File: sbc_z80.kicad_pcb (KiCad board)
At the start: 2 copper layers, 101.6 x 50.8 mm, 19 parts, among them J1 Conn_02x40_Top_Bottom, J2 UPDI TTL, U1 Z84C4310AEG, U10 74HC3G34DP,125, U2 Si5351A-B-GT, U3 IS62C5128BL-45TLI, U4 27C512PLCC, U5 ATtiny1614-SS, U6 Z84C0010AEG, U7 EPM7032STC44, U8 Z84C3010AEG, U9 Z84C2010AEG, Y1 25MHZ 8PF

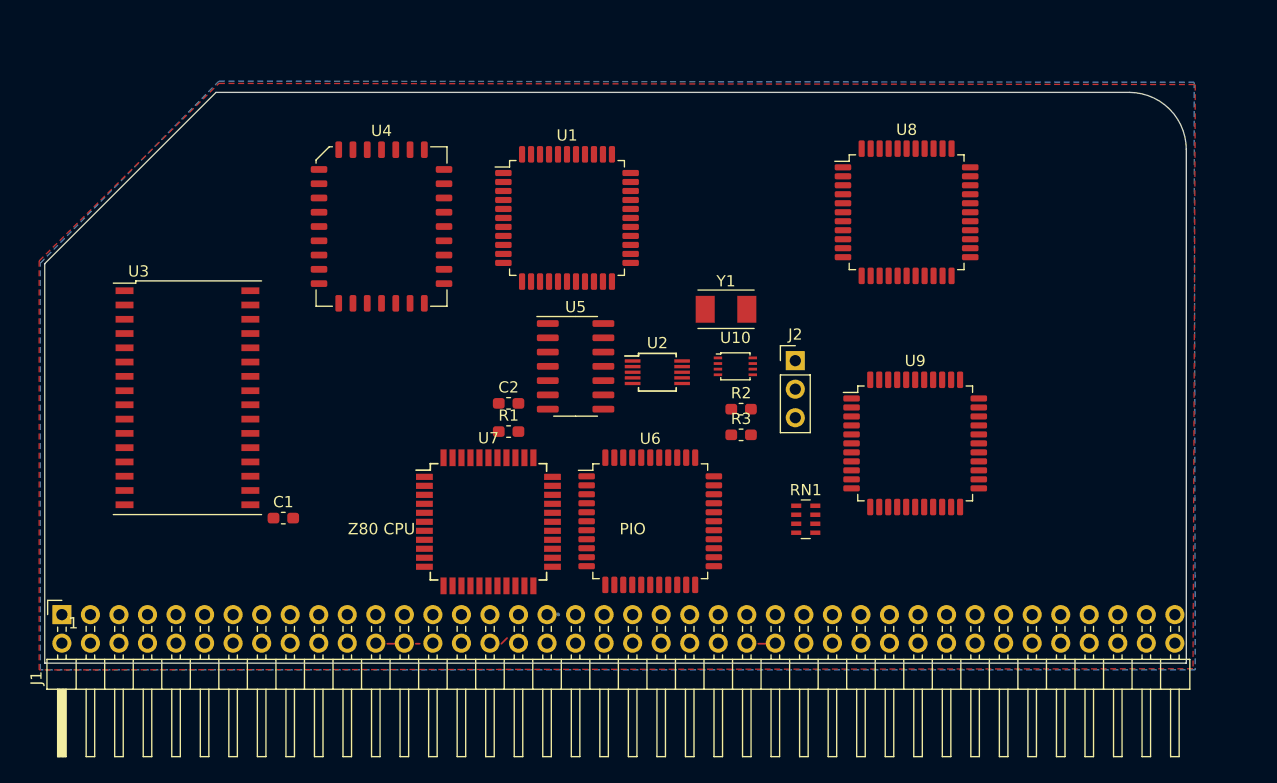
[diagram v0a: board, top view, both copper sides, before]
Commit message: added 3V3 section for clock generator
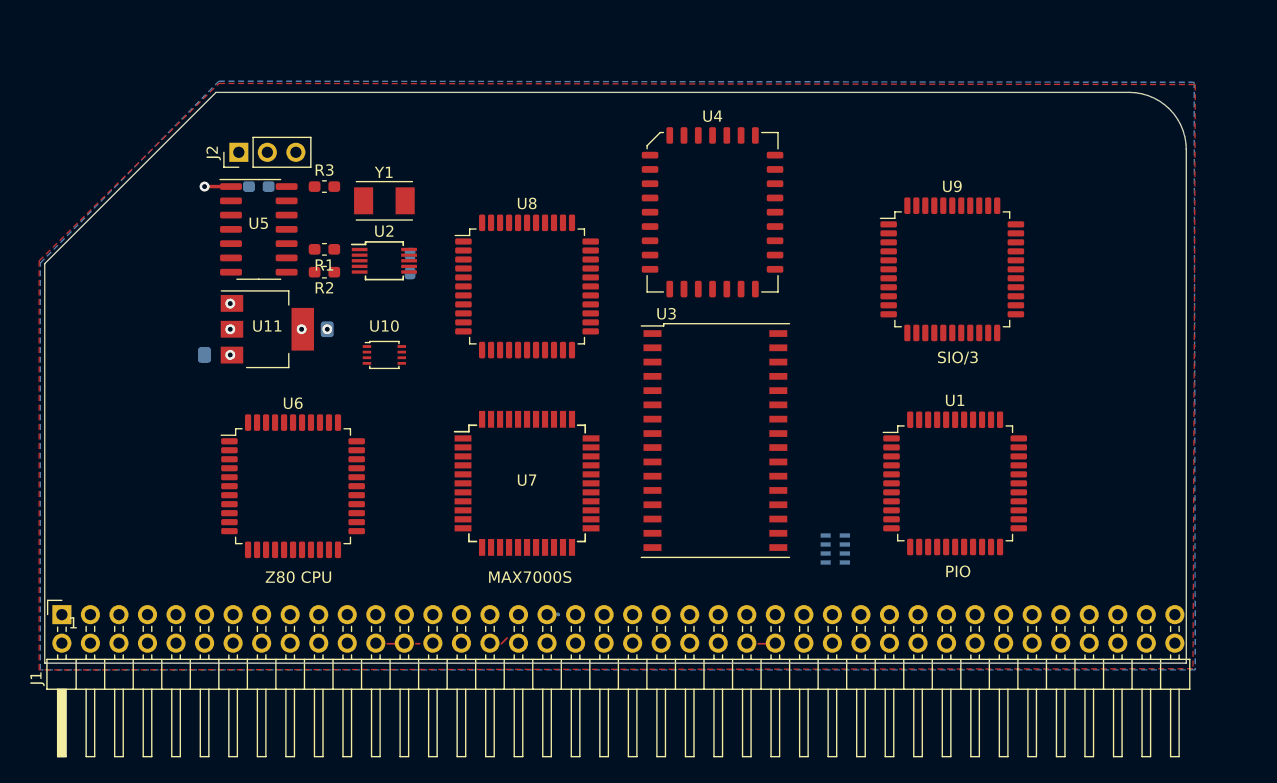
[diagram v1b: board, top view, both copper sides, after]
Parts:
- added C3: 10uF, Capacitor_SMD:C_0805_2012Metric_Pad1.15x1.40mm_HandSolder, B.Cu at (90.7, 100.1)
- added C4: 22uF, Capacitor_SMD:C_0805_2012Metric_Pad1.15x1.40mm_HandSolder, B.Cu at (99.6, 97.8)
- added U11: AZ1117CH-3.3TRG1, Package_TO_SOT_SMD:SOT-223-3_TabPin2, F.Cu at (95.2, 97.8)
- C1, C2, RN1: moved to B.Cu
- moved J2 52.9 mm to (92.7, 82.0), turned to 90 degrees
- moved U3 47.1 mm to (135.1, 107.7)
- moved R3 43.2 mm to (100.3, 85.1)
- moved U1 41.8 mm to (156.5, 111.5)
- moved R2 39.0 mm to (100.3, 92.7), turned to 180 degrees
- moved U8 34.4 mm to (118.4, 94.0)
- moved U6 31.9 mm to (97.5, 111.8)
- moved Y1 31.9 mm to (105.7, 86.4)
- moved U10 31.3 mm to (105.7, 100.1)
- moved U5 30.7 mm to (94.5, 88.9)
- moved U4 29.5 mm to (134.9, 87.4)
- moved C2 29.4 mm to (94.5, 85.1)
- moved U2 26.2 mm to (105.7, 91.7)
- moved C1 25.3 mm to (108.0, 91.9), turned to 90 degrees
- moved R1 23.1 mm to (100.3, 90.7), turned to 180 degrees
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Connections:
- J1 pad 23: (no net) -> /~MREQ
- J1 pad 24: (no net) -> /~WR
- J1 pad 25: (no net) -> /~RD
- J1 pad 26: (no net) -> /~IORQ
- J1 pad 54: (no net) -> /A18
- J1 pad 55: (no net) -> /A17
- J1 pad 56: (no net) -> /A16
- U1 pad 20: (no net) -> /A0
- U1 pad 21: (no net) -> /A1
- U1 pad 5: (no net) -> /CLK
- U3 pad 1: (no net) -> /A17
- U3 pad 2: (no net) -> /A16
- U3 pad 30: (no net) -> /A18
- U7 pad 1: /A3 -> (no net)
- U7 pad 10: (no net) -> /~RD
- U7 pad 11: (no net) -> /~WR
- U7 pad 12: (no net) -> /~MREQ
- U7 pad 13: (no net) -> /A7
- U7 pad 14: (no net) -> /A7
- U7 pad 15: (no net) -> /A7
- U7 pad 2: /A4 -> /A3
- U7 pad 3: /A5 -> /A4
- U7 pad 5: /A6 -> /A5
- U7 pad 6: /A7 -> /A6
- U7 pad 8: (no net) -> /~IORQ
- U9 pad 11: (no net) -> /A1
- U9 pad 12: (no net) -> /A0
- U9 pad 33: (no net) -> /CLK
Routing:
- net 3V3: track 0.00 -> 2.35 mm, vias 0 -> 3
- net GND: vias 0 -> 2
- net 5V: vias 0 -> 1
- added copper zone on In2.Cu, net 3V3
- added copper zone on In2.Cu, net 5V
- added copper zone on In1.Cu, net GND
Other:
- copper layers 2 -> 4
- board text added: "MAX7000S"
- board text added: "SIO/3"

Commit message: larger sheet, connected more pins
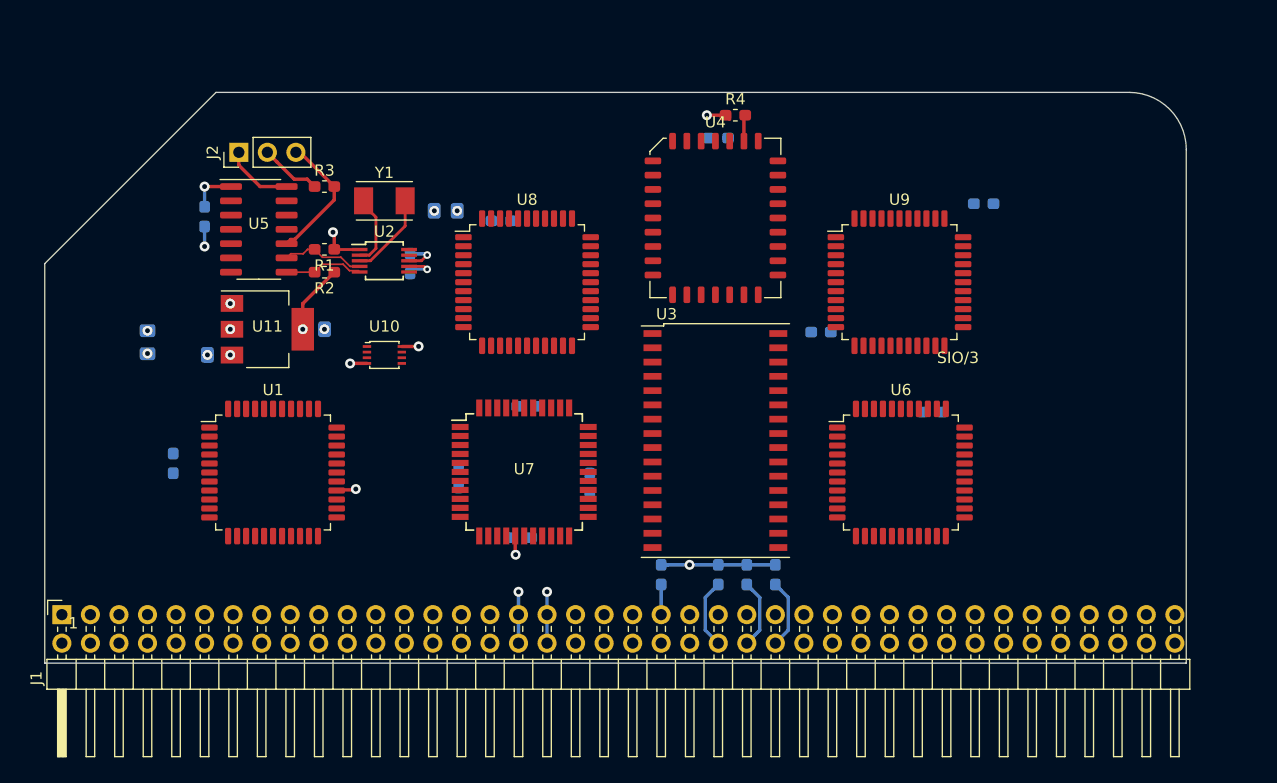
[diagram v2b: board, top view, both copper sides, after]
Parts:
- removed RN1: 10K, Resistor_SMD:R_Array_Concave_4x0603
- added C10: 100nF, Capacitor_SMD:C_0603_1608Metric_Pad1.05x0.95mm_HandSolder, B.Cu at (144.5, 98.0)
- added C11: 100nF, Capacitor_SMD:C_0603_1608Metric_Pad1.05x0.95mm_HandSolder, B.Cu at (154.4, 105.2)
- added C12: 100nF, Capacitor_SMD:C_0603_1608Metric_Pad1.05x0.95mm_HandSolder, B.Cu at (159.0, 86.6)
- added C13: 100nF, Capacitor_SMD:C_0603_1608Metric_Pad1.05x0.95mm_HandSolder, B.Cu at (135.4, 80.8)
- added C14: 100nF, Capacitor_SMD:C_0603_1608Metric_Pad1.05x0.95mm_HandSolder, B.Cu at (116.1, 88.1)
- added C15: 100nF, Capacitor_SMD:C_0805_2012Metric_Pad1.15x1.40mm_HandSolder, B.Cu at (84.6, 98.9)
- added C16: 100nF, Capacitor_SMD:C_0805_2012Metric_Pad1.15x1.40mm_HandSolder, B.Cu at (111.1, 87.2)
- added C5: 100nF, Capacitor_SMD:C_0603_1608Metric_Pad1.05x0.95mm_HandSolder, B.Cu at (118.4, 104.6)
- added C6: 100nF, Capacitor_SMD:C_0603_1608Metric_Pad1.05x0.95mm_HandSolder, B.Cu at (112.3, 111.0)
- added C7: 100nF, Capacitor_SMD:C_0603_1608Metric_Pad1.05x0.95mm_HandSolder, B.Cu at (124.0, 111.5)
- added C8: 100nF, Capacitor_SMD:C_0603_1608Metric_Pad1.05x0.95mm_HandSolder, B.Cu at (117.9, 116.3)
- added C9: 100nF, Capacitor_SMD:C_0603_1608Metric_Pad1.05x0.95mm_HandSolder, B.Cu at (86.9, 109.7)
- added R4: 10K, Resistor_SMD:R_0603_1608Metric_Pad1.05x0.95mm_HandSolder, F.Cu at (136.9, 78.7)
- added R5: 10K, Resistor_SMD:R_0603_1608Metric_Pad1.05x0.95mm_HandSolder, B.Cu at (130.3, 119.6)
- added R6: 10K, Resistor_SMD:R_0603_1608Metric_Pad1.05x0.95mm_HandSolder, B.Cu at (140.5, 119.6)
- added R7: 10K, Resistor_SMD:R_0603_1608Metric_Pad1.05x0.95mm_HandSolder, B.Cu at (137.9, 119.6)
- added R8: 10K, Resistor_SMD:R_0603_1608Metric_Pad1.05x0.95mm_HandSolder, B.Cu at (135.4, 119.6)
- J1: value Conn_02x40_Top_Bottom -> RC80 Bus
- U1: value Z84C4310AEG -> CPU - Z84C0010AEG
- U3: value IS62C5128BL-45TLI -> SRAM - IS62C5128BL-45TLI
- U4: value 27C512PLCC -> ROM - GLS29EE512
- U6: value Z84C0010AEG -> SIO/3 - Z84C4310AEG
- U7: value EPM7032STC44 -> CPLD - EPM7032STC44
- U8: value Z84C3010AEG -> CTC - Z84C3010AEG
- U9: value Z84C2010AEG -> PIO - Z84C2010AEG
- moved U1 60.7 mm to (95.8, 110.5)
- moved U6 54.1 mm to (151.6, 110.5)
- moved C2 5.52 mm to (89.7, 87.8), turned to 270 degrees
- moved U9 4.84 mm to (151.5, 93.6)
- moved U7 1.05 mm to (118.1, 110.5)
- moved U4 0.57 mm to (135.1, 87.9)
- moved U8 0.38 mm to (118.4, 93.6)
- moved C3 0.26 mm to (90.9, 100.1)
- moved C4 0.25 mm to (99.3, 97.8)
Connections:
- net 3V3 renamed +3V3
- C3 pad 1: 5V -> +5V
- J1 pad 18: 5V -> +5V
- J1 pad 19: (no net) -> /~M1
- J1 pad 20: (no net) -> /~RESET
- J1 pad 40: (no net) -> /IEO
- J1 pad 58: 5V -> +5V
- J1 pad 62: (no net) -> /~BUSACK
- J1 pad 63: (no net) -> /~HALT
- J1 pad 64: /~BUSRQ -> /~BUSREQ
- J1 pad 80: (no net) -> /IEI
- U1 pad 1: (no net) -> /CLK
- U1 pad 10: (no net) -> /D1
- U1 pad 11: (no net) -> Net-(U1-Pad11)
- U1 pad 12: (no net) -> /~INT
- U1 pad 13: (no net) -> /~NMI
- U1 pad 14: (no net) -> /~HALT
- U1 pad 15: (no net) -> /~MREQ
- U1 pad 16: (no net) -> /~IORQ
- U1 pad 17: Net-(U1-Pad17) -> Net-(U1-Pad11)
- U1 pad 18: GND -> /~RD
- U1 pad 19: (no net) -> /~WR
- U1 pad 2: (no net) -> /D4
- U1 pad 20: /A0 -> /~BUSACK
- U1 pad 21: /A1 -> /~WAIT
- U1 pad 22: (no net) -> /~BUSREQ
- U1 pad 23: (no net) -> /~RESET
- U1 pad 24: /D6 -> /~M1
- U1 pad 25: /D4 -> (no net)
- U1 pad 26: /D2 -> GND
- U1 pad 27: /D0 -> /A0
- U1 pad 28: Net-(U1-Pad17) -> /A1
- U1 pad 29: /D1 -> /A2
- U1 pad 3: (no net) -> /D3
- U1 pad 30: /D3 -> /A3
- U1 pad 31: /D5 -> /A4
- U1 pad 32: /D7 -> /A5
- U1 pad 33: (no net) -> Net-(U1-Pad11)
- U1 pad 34: (no net) -> /A6
- U1 pad 35: (no net) -> /A7
- U1 pad 36: (no net) -> /A8
- U1 pad 37: 5V -> /A9
- U1 pad 38: (no net) -> /A10
- U1 pad 39: Net-(U1-Pad17) -> Net-(U1-Pad11)
- U1 pad 4: (no net) -> /D5
- U1 pad 40: (no net) -> /A11
- U1 pad 41: (no net) -> /A12
- U1 pad 42: (no net) -> /A13
- U1 pad 43: (no net) -> /A14
- U1 pad 44: (no net) -> /A15
- U1 pad 5: /CLK -> /D6
- U1 pad 6: (no net) -> +5V
- U1 pad 7: (no net) -> /D2
- U1 pad 8: (no net) -> /D7
- U1 pad 9: (no net) -> /D0
- U10 pad 8: 5V -> +5V
- U11 pad 3: 5V -> +5V
- U3 pad 24: (no net) -> /~RD
- U3 pad 29: (no net) -> /~WR
- U3 pad 32: 5V -> +5V
- U4 pad 1: (no net) -> Net-(U4-Pad1)
- U4 pad 10: /A1 -> /A2
- U4 pad 11: /A0 -> /A1
- U4 pad 12: (no net) -> /A0
- U4 pad 16: (no net) -> GND
- U4 pad 17: (no net) -> /D3
- U4 pad 18: /D3 -> /D4
- U4 pad 19: /D4 -> /D5
- U4 pad 2: /A15 -> Net-(U4-Pad1)
- U4 pad 20: /D5 -> /D6
- U4 pad 21: /D6 -> /D7
- U4 pad 22: /D7 -> (no net)
- U4 pad 23: (no net) -> /A10
- U4 pad 24: /A10 -> /~RD
- U4 pad 25: (no net) -> /A11
- U4 pad 26: (no net) -> /A9
- U4 pad 27: /A11 -> /A8
- U4 pad 28: /A9 -> /A13
- U4 pad 29: /A8 -> /A14
- U4 pad 3: /A12 -> /A15
- U4 pad 30: /A13 -> Net-(U4-Pad1)
- U4 pad 31: /A14 -> Net-(R4-Pad2)
- U4 pad 32: 5V -> +5V
- U4 pad 4: /A7 -> /A12
- U4 pad 5: /A6 -> /A7
- U4 pad 6: /A5 -> /A6
- U4 pad 7: /A4 -> /A5
- U4 pad 8: /A3 -> /A4
- U4 pad 9: /A2 -> /A3
- U6 pad 10: /D1 -> (no net)
- U6 pad 17: (no net) -> Net-(U6-Pad17)
- U6 pad 18: (no net) -> GND
- U6 pad 19: (no net) -> /~RD
- U6 pad 2: /D4 -> (no net)
- U6 pad 20: (no net) -> /A0
- U6 pad 21: (no net) -> /A1
- U6 pad 23: (no net) -> /~IORQ
- U6 pad 24: (no net) -> /D6
- U6 pad 25: (no net) -> /D4
- U6 pad 26: GND -> /D2
- U6 pad 27: /A0 -> /D0
- U6 pad 28: /A1 -> Net-(U6-Pad17)
- U6 pad 29: /A2 -> /D1
- U6 pad 3: /D3 -> (no net)
- U6 pad 30: /A3 -> /D3
- U6 pad 31: /A4 -> /D5
- U6 pad 32: /A5 -> /D7
- U6 pad 33: (no net) -> /~INT
- U6 pad 34: /A6 -> /IEI
- U6 pad 35: /A7 -> /IEO
- U6 pad 36: /A8 -> /~M1
- U6 pad 37: /A9 -> +5V
- U6 pad 38: /A10 -> (no net)
- U6 pad 39: (no net) -> Net-(U6-Pad17)
- U6 pad 4: /D5 -> (no net)
- U6 pad 40: /A11 -> (no net)
- U6 pad 41: /A12 -> (no net)
- U6 pad 42: /A13 -> (no net)
- U6 pad 43: /A14 -> (no net)
- U6 pad 44: /A15 -> (no net)
- U6 pad 5: /D6 -> /CLK
- U6 pad 6: 5V -> /~RESET
- U6 pad 7: /D2 -> (no net)
- U6 pad 8: /D7 -> (no net)
- U6 pad 9: /D0 -> (no net)
- U7 pad 10: /~RD -> /~IORQ
- U7 pad 11: /~WR -> /~MREQ
- U7 pad 12: /~MREQ -> /~RD
- U7 pad 13: /A7 -> /~WR
- U7 pad 14: /A7 -> (no net)
- U7 pad 15: /A7 -> (no net)
- U7 pad 17: 5V -> +5V
- U7 pad 29: 5V -> +5V
- U7 pad 41: 5V -> +5V
- U7 pad 8: /~IORQ -> /A7
- U7 pad 9: 5V -> +5V
- U8 pad 22: (no net) -> /IEI
- U8 pad 23: (no net) -> /IEO
- U8 pad 25: (no net) -> /~INT
- U8 pad 29: (no net) -> /CLK
- U8 pad 32: (no net) -> /~RESET
- U8 pad 43: 5V -> +5V
- U9 pad 1: (no net) -> /~IORQ
- U9 pad 3: (no net) -> /~M1
- U9 pad 30: (no net) -> /IEO
- U9 pad 31: (no net) -> /~INT
- U9 pad 32: (no net) -> /IEI
- U9 pad 34: 5V -> +5V
- U9 pad 44: (no net) -> /~RD
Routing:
- net GND: track 0.00 -> 20.9 mm, vias 2 -> 9
- net +5V: track 0.00 -> 18.4 mm, vias 0 -> 7
- net +3V3: track 2.35 -> 18.5 mm, vias 3 -> 7
- net /Clocks/RX: track 0.00 -> 11.7 mm
- net Net-(U2-Pad3): track 0.00 -> 7.57 mm
- net Net-(R1-Pad2): track 0.00 -> 7.44 mm
- net Net-(R2-Pad2): track 0.00 -> 7.08 mm
- net Net-(U2-Pad2): track 0.00 -> 6.39 mm
- net /~WAIT: track 0.00 -> 6.18 mm
- net /~BUSREQ: track 0.00 -> 6.18 mm
- net /Clocks/TX: track 0.00 -> 5.47 mm
- net /~NMI: track 0.71 -> 6.18 mm
- net /~INT: track 0.00 -> 2.68 mm
- net Net-(R4-Pad2): track 0.00 -> 2.35 mm
- net (no net): track 1.81 -> 0.00 mm
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- added copper zone on In2.Cu, net +5V
- removed copper zone on In2.Cu, net 5V
- removed copper zone on B.Cu, net GND
- removed copper zone on F.Cu, net GND
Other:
- net class Net-(D1-Pad1)	Defaultr removed
- net class Power removed
- board text removed: "MAX7000S"
- board text removed: "PIO"
- board text removed: "Z80 CPU"

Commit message: started routing
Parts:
- added J3: Conn_02x12_Odd_Even, Connector_PinHeader_2.54mm:PinHeader_2x12_P2.54mm_Horizontal, F.Cu at (170.4, 90.7)
- added J4: Conn_01x06, Connector_PinHeader_2.54mm:PinHeader_1x06_P2.54mm_Horizontal, F.Cu at (141.9, 81.0)
- added J5: Conn_01x06, Connector_PinHeader_2.54mm:PinHeader_1x06_P2.54mm_Horizontal, F.Cu at (159.0, 80.9)
- R4: moved to B.Cu
- moved C10 10.4 mm to (134.1, 98.3), turned to 180 degrees
- moved R4 6.25 mm to (134.1, 84.3)
- moved C7 2.82 mm to (121.2, 111.9)
- moved C1 2.67 mm to (105.3, 92.1)
- moved C16 2.67 mm to (108.5, 87.4)
- moved C3 2.67 mm to (88.3, 100.2)
- moved C5 2.67 mm to (115.7, 104.8)
- moved C8 2.67 mm to (115.2, 116.5)
- moved R1 2.67 mm to (97.7, 90.8)
- moved R2 2.67 mm to (97.7, 92.8)
- moved U10 2.67 mm to (103.0, 100.2)
- moved U7 2.67 mm to (115.4, 110.6)
- moved C13 2.67 mm to (132.7, 80.9)
- moved C14 2.67 mm to (113.4, 88.3)
- moved C2 2.67 mm to (87.0, 87.9)
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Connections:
- U3 pad 22: (no net) -> /RAM_CE
- U7 pad 21: (no net) -> /~WAIT
- U7 pad 22: (no net) -> /~HALT
- U7 pad 35: (no net) -> /RAM_CE
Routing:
- net /A15: track 0.00 -> 111.6 mm, vias 0 -> 4
- net /~RESET: track 0.00 -> 65.4 mm, vias 0 -> 4
- net /~MREQ: track 0.00 -> 55.2 mm, vias 0 -> 4
- net /~WR: track 0.00 -> 44.0 mm
- net /A0: track 0.00 -> 43.0 mm, vias 0 -> 4
- net /A1: track 0.00 -> 42.7 mm, vias 0 -> 4
- net /~BUSREQ: track 6.18 -> 47.2 mm, vias 0 -> 1
- net /~BUSACK: track 0.00 -> 40.3 mm, vias 0 -> 1
- net /~M1: track 0.00 -> 33.7 mm, vias 0 -> 3
- net /~INT: track 2.68 -> 33.8 mm, vias 0 -> 1
- net /A14: track 0.00 -> 28.6 mm, vias 0 -> 1
- net /A3: track 0.00 -> 26.9 mm, vias 0 -> 2
- net /A4: track 0.00 -> 26.0 mm, vias 0 -> 1
- net /A2: track 0.00 -> 23.5 mm, vias 0 -> 1
- net +5V: track 18.4 -> 40.9 mm, vias 7 -> 13
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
